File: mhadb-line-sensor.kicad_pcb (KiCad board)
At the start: 2 copper layers, 100 x 20 mm, 115 parts, among them J1 TC2030, J2 Conn_01x04_Pin, J3 Conn_01x04, J4 Conn_01x04_Pin, SW1 SW_Push, SW2 SW_Push, SW3 SW_Push, SW4 SW_Push, SW5 SW_Push, U1 HT753-1, U10 QRE1113GR, U11 QRE1113GR, U12 QRE1113GR, U13 QRE1113GR, U2 SN65HVD230, U3 STM32F103C8Tx, U4 QRE1113GR, U5 QRE1113GR, U6 QRE1113GR, U7 QRE1113GR, U8 QRE1113GR, U9 QRE1113GR, Y1 8M

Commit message: pcb: initial rough layout
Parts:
- removed FID1, FID2, FID3: Fiducial, Fiducial:Fiducial_1mm_Mask2mm
- removed H3, H4, H5: MountingHole, MountingHole:ToolingHole_1.152mm
- removed SW5: SW_Push, Button_Switch_THT:SW_SPST_Omron_B3F-40xx
- removed TP3, TP5, TP6: TestPoint, TestPoint:TestPoint_Pad_D2.0mm
- R12, R13, R14, R15, R16, R17, R19, R20, R21: footprint Capacitor_SMD:C_1206_3216Metric -> Resistor_SMD:R_1206_3216Metric
- R18: footprint Capacitor_SMD:C_1206_3216Metric -> Resistor_SMD:R_1206_3216Metric; moved to B.Cu
- R23, TP8, TP9: moved to B.Cu
- moved D21 163.1 mm to (203.4, 99.0), turned to 90 degrees
- moved TP2 156.8 mm to (204.0, 86.5), turned to 90 degrees
- moved D19 148.9 mm to (193.5, 99.0), turned to 90 degrees
- moved D7 141.9 mm to (201.5, 85.5), turned to 90 degrees
- moved D15 140.6 mm to (173.5, 99.0), turned to 90 degrees
- moved J1 139.6 mm to (194.6, 88.0), turned to -90 degrees
- moved U2 137.1 mm to (148.3, 92.8), turned to 180 degrees
- moved D17 135.1 mm to (183.5, 99.0), turned to 90 degrees
- moved D6 132.0 mm to (192.0, 87.5), turned to 90 degrees
- moved D5 131.3 mm to (191.5, 86.0), turned to 180 degrees
- moved D4 130.7 mm to (191.5, 85.0), turned to 180 degrees
- moved D2 129.1 mm to (135.0, 88.5), turned to 180 degrees
- moved D3 126.7 mm to (192.0, 90.0), turned to -90 degrees
- moved D13 126.1 mm to (163.5, 99.0), turned to 90 degrees
- moved SW4 116.9 mm to (168.5, 99.0), turned to -90 degrees
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
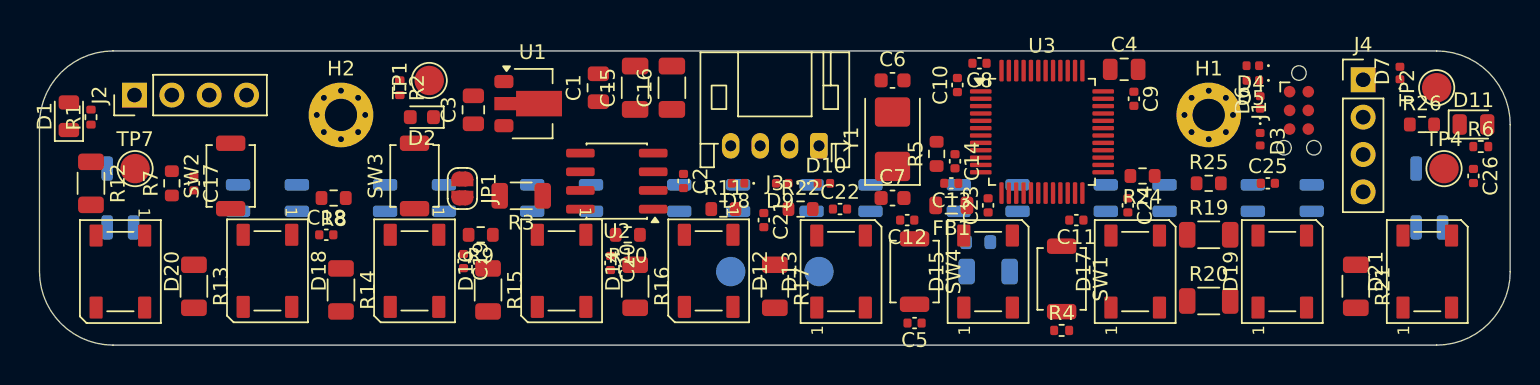
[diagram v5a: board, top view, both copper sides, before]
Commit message: pcb: add gnd planes
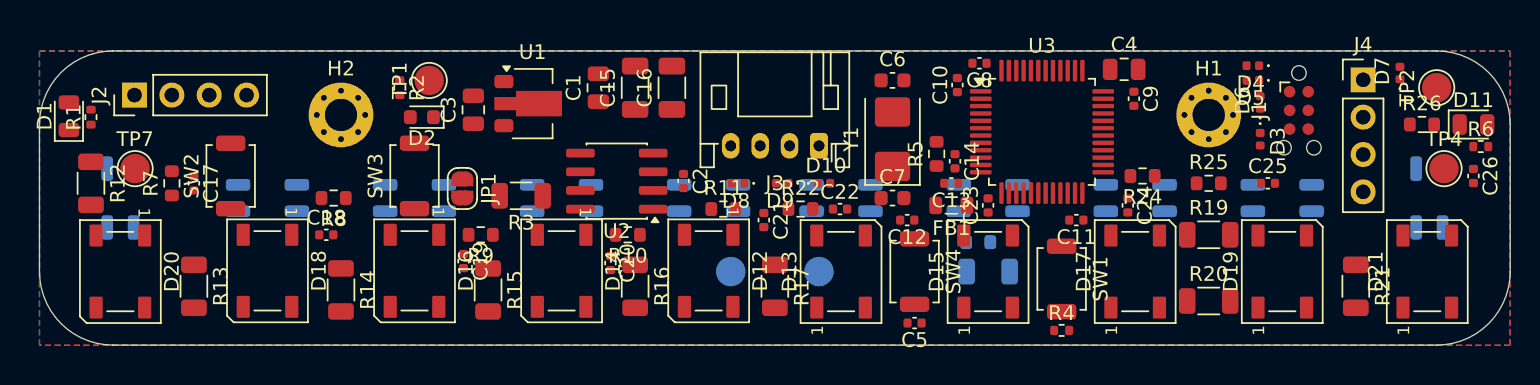
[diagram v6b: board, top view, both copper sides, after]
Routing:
- added copper zone on B.Cu, net GND
- added copper zone on F.Cu, net GND
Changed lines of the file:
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@@
 		(layer "Edge.Cuts")
+	)
+	(zone
+		(net 2)
+		(net_name "GND")
+		(layers "F.Cu" "B.Cu")
+		(hatch edge 0.5)
+		(connect_pads
+			(clearance 0.2)
+		)
+		(min_thickness 0.15)
+		(filled_areas_thickness no)
+		(fill yes
+			(thermal_gap 0.35)
+			(thermal_bridge_width 0.35)
+		)
+		(polygon
+			(pts
+				(xy 109 84) (xy 209 84) (xy 209 104) (xy 109 104)
+			)
+		)
 	)
 	(embedded_fonts no)

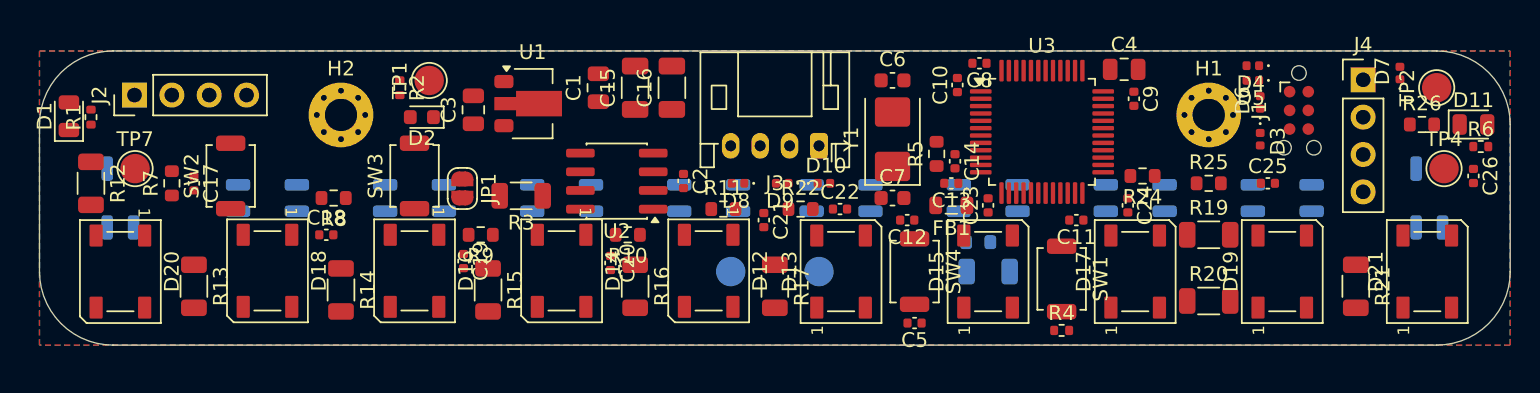
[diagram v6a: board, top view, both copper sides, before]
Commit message: pcb: add gnd vias
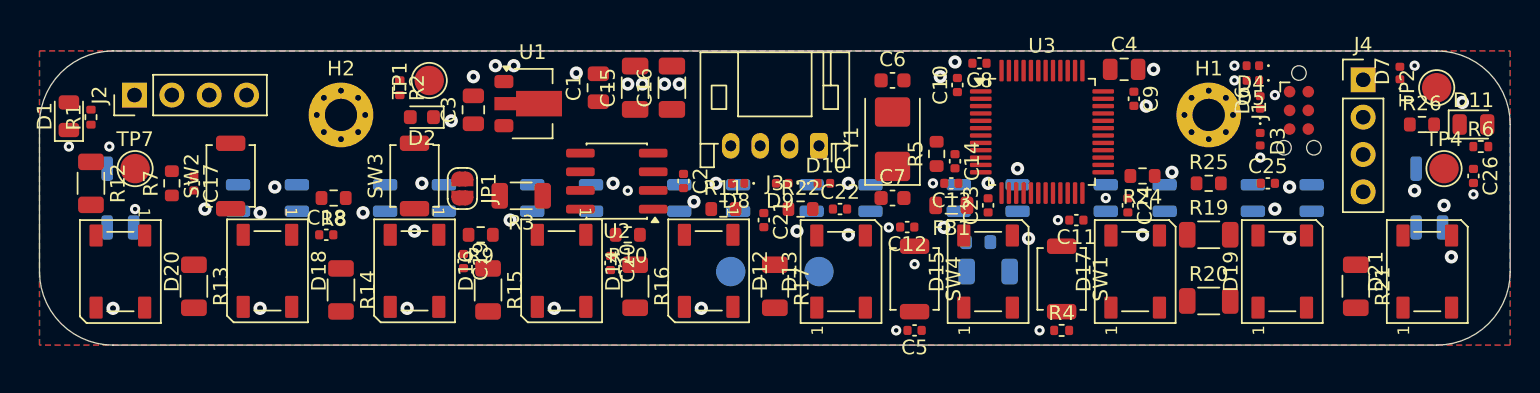
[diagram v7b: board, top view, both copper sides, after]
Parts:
- moved C5 0.50 mm to (168.5, 103.0)
- moved SW4 0.50 mm to (168.5, 99.5)
- moved C12 0.47 mm to (168.0, 96.0)
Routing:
- net GND: vias 0 -> 61

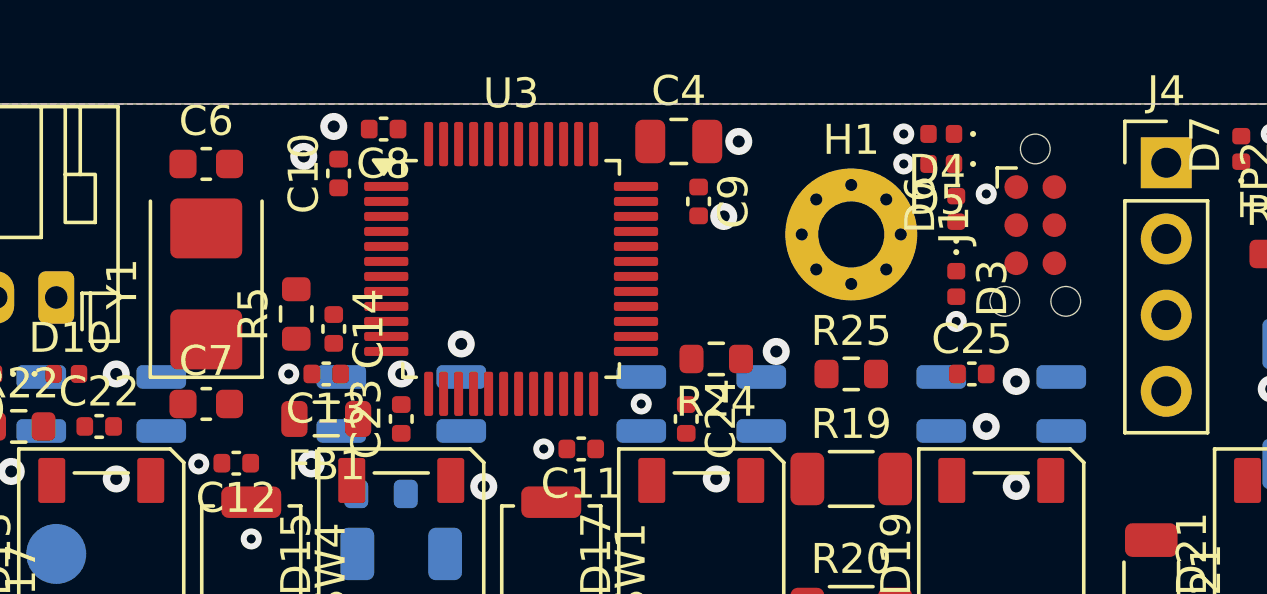
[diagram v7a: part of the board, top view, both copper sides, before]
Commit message: pcb: add SWD routing
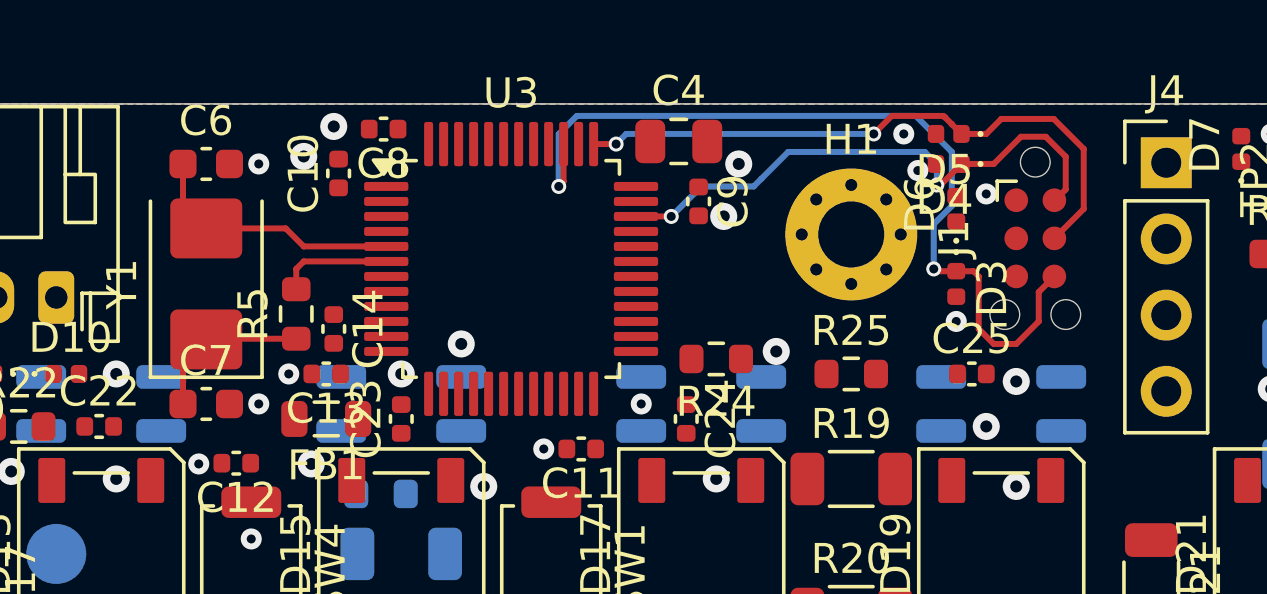
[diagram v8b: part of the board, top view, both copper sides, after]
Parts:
- moved D4 1.03 mm to (191.8, 86.0)
- moved D5 1.03 mm to (191.8, 85.0)
- moved J1 0.44 mm to (194.6, 88.5)
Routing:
- net /SWO: track 0.00 -> 28.8 mm, vias 0 -> 2
- net /SWCLK: track 0.00 -> 21.0 mm, vias 0 -> 2
- net /SWDIO: track 0.00 -> 18.7 mm, vias 0 -> 2
- net /XTAL_I: track 0.00 -> 8.72 mm
- net /XTAL_RO: track 0.00 -> 5.48 mm
- net /XTAL_O: track 0.00 -> 3.78 mm
- net GND: vias 61 -> 63
